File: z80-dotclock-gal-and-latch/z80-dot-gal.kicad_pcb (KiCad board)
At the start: 2 copper layers, 30.5 x 83.2 mm, 12 parts, among them J1 Board corner fix, J2 EXP_PORT, J3 GAL_1_9, J4 GAL_11_19, U1 Z80CPU SOCKET PINS, U2 Z80CPU, U3 GAL16V8

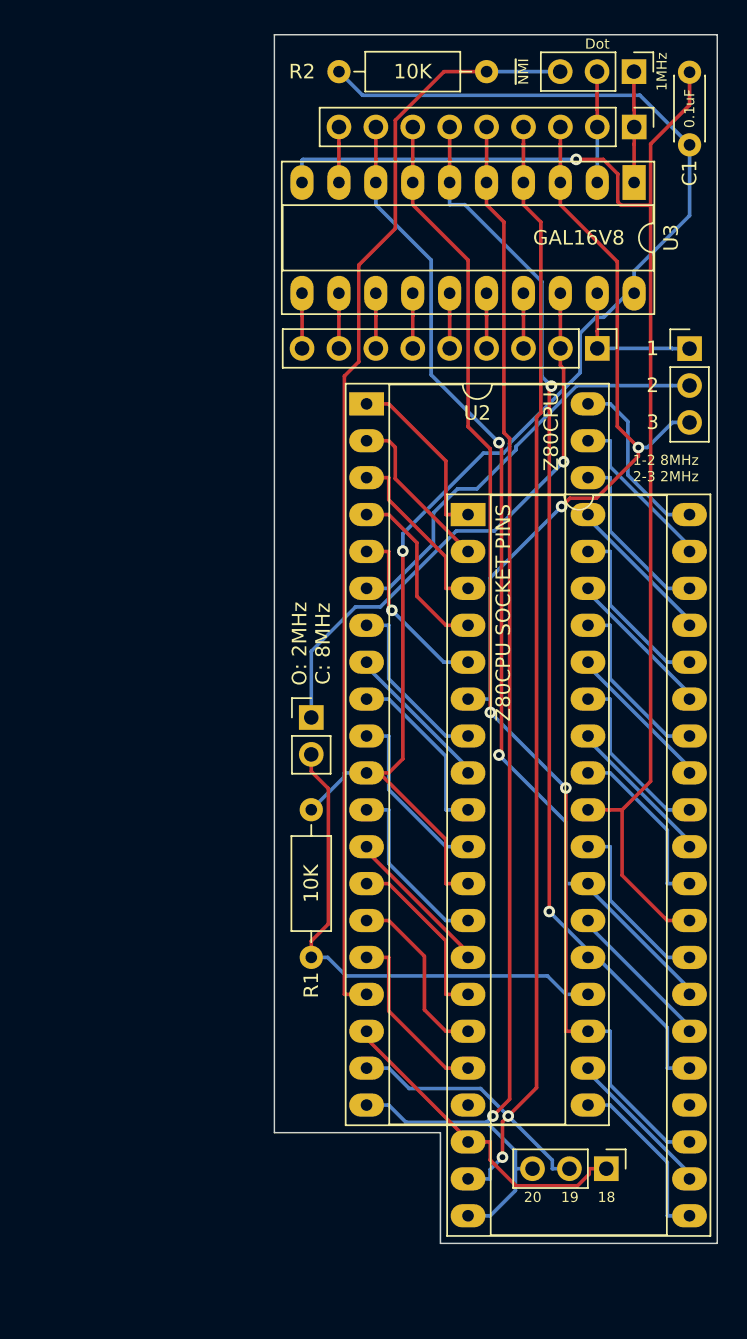
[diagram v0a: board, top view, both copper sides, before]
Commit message: Schematic revision v2, without PCB: - remove test pads - remove unused connections to GAL pins 6-8 - add J3 and lots of descriptions - add required connects to /WR, /RESET, /RFSH - make GAL socket compatible with 16V8
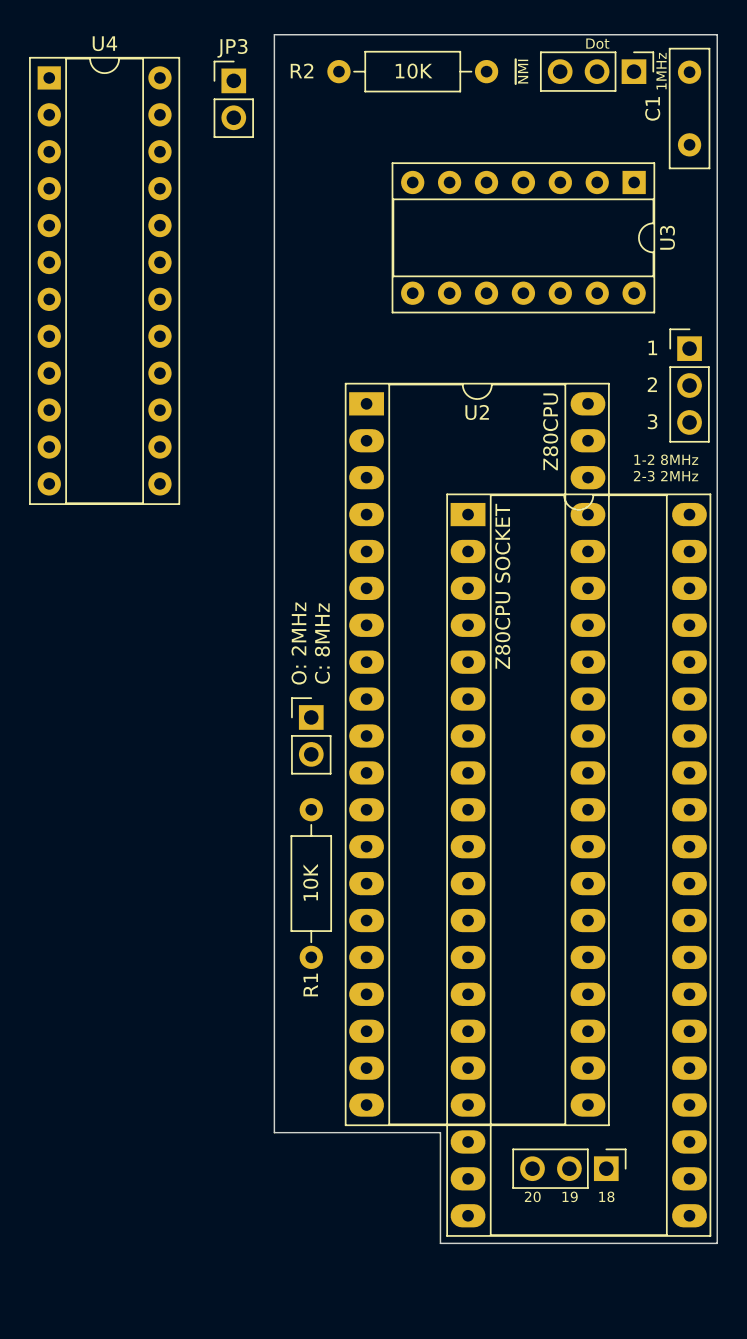
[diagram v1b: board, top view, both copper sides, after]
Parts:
- removed J3: GAL_1_9, Connector_PinHeader_2.54mm:PinHeader_1x09_P2.54mm_Vertical
- removed J4: GAL_11_19, Connector_PinHeader_2.54mm:PinHeader_1x09_P2.54mm_Vertical
- added JP3: FAST/SLOW, Connector_PinHeader_2.54mm:PinHeader_1x02_P2.54mm_Vertical, F.Cu at (111.5, 52.1)
- added U4: GAL22V10, Package_DIP:DIP-24_W7.62mm_Socket, F.Cu at (98.8, 51.9)
- C1: footprint Capacitor_THT:C_Disc_D4.3mm_W1.9mm_P5.00mm -> Capacitor_THT:C_Disc_D8.0mm_W2.5mm_P5.00mm
- U1: value Z80CPU SOCKET PINS -> Z80CPU SOCKET
- U3: value GAL16V8 -> 74LS74; footprint Package_DIP:DIP-20_W7.62mm_Socket_LongPads -> Package_DIP:DIP-14_W7.62mm_Socket
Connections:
- U3 pad 1: /CLK1MHZ -> /~{WAITRESET}
- U3 pad 10: GND -> VCC
- U3 pad 11: Net-(J4-Pad9) -> GND
- U3 pad 12: Net-(J4-Pad8) -> GND
- U3 pad 13: Net-(J4-Pad7) -> VCC
- U3 pad 14: Net-(J4-Pad6) -> VCC
- U3 pad 2: /DOTCLK -> VCC
- U3 pad 3: /~{CLK_IN} -> /WAITTRIGGER
- U3 pad 4: /~{MREQ} -> VCC
- U3 pad 5: /~{IORQ} -> unconnected-(U3-Pad5)
- U3 pad 6: /~{BUSRQ} -> /WAITLATCH
- U3 pad 7: /~{BUSACK} -> GND
- U3 pad 8: /~{M1} -> unconnected-(U3-Pad8)
- U3 pad 9: Net-(J3-Pad9) -> unconnected-(U3-Pad9)
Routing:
- net VCC: track 97.1 -> 0.00 mm, vias 1 -> 0
- net GND: track 93.5 -> 0.00 mm, vias 1 -> 0
- net /~{MREQ}: track 93.0 -> 0.00 mm, vias 2 -> 0
- net /~{IORQ}: track 89.2 -> 0.00 mm, vias 1 -> 0
- net /~{BUSACK}: track 81.2 -> 0.00 mm, vias 2 -> 0
- net /~{NMI}: track 75.9 -> 0.00 mm
- net /~{BUSRQ}: track 74.0 -> 0.00 mm, vias 2 -> 0
- net /~{M1}: track 69.7 -> 0.00 mm, vias 2 -> 0
- net /~{CLK_IN}: track 52.7 -> 0.00 mm, vias 2 -> 0
- net /~{WAITOUT}: track 39.0 -> 0.00 mm, vias 1 -> 0
- net /~{WAIT}: track 35.0 -> 0.00 mm
- net Net-(JP2-Pad2): track 29.4 -> 0.00 mm
- net /~{HALT}: track 22.7 -> 0.00 mm
- net /A15: track 12.4 -> 0.00 mm, vias 1 -> 0
- net /~{RD}: track 12.3 -> 0.00 mm
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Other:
- board text added: "C128 Z80 @ 8MHz V2.0 Maciej Witkowiak, <ytm@elysium.pl> VI 2024"
- board text removed: "C128 Z80 @ 8MHz dev board V1.0 Maciej Witkowiak, <ytm@elysium.pl> VIII 2023"

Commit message: C128D/DCR PCB project (without cutout for 256k MMU expansion)
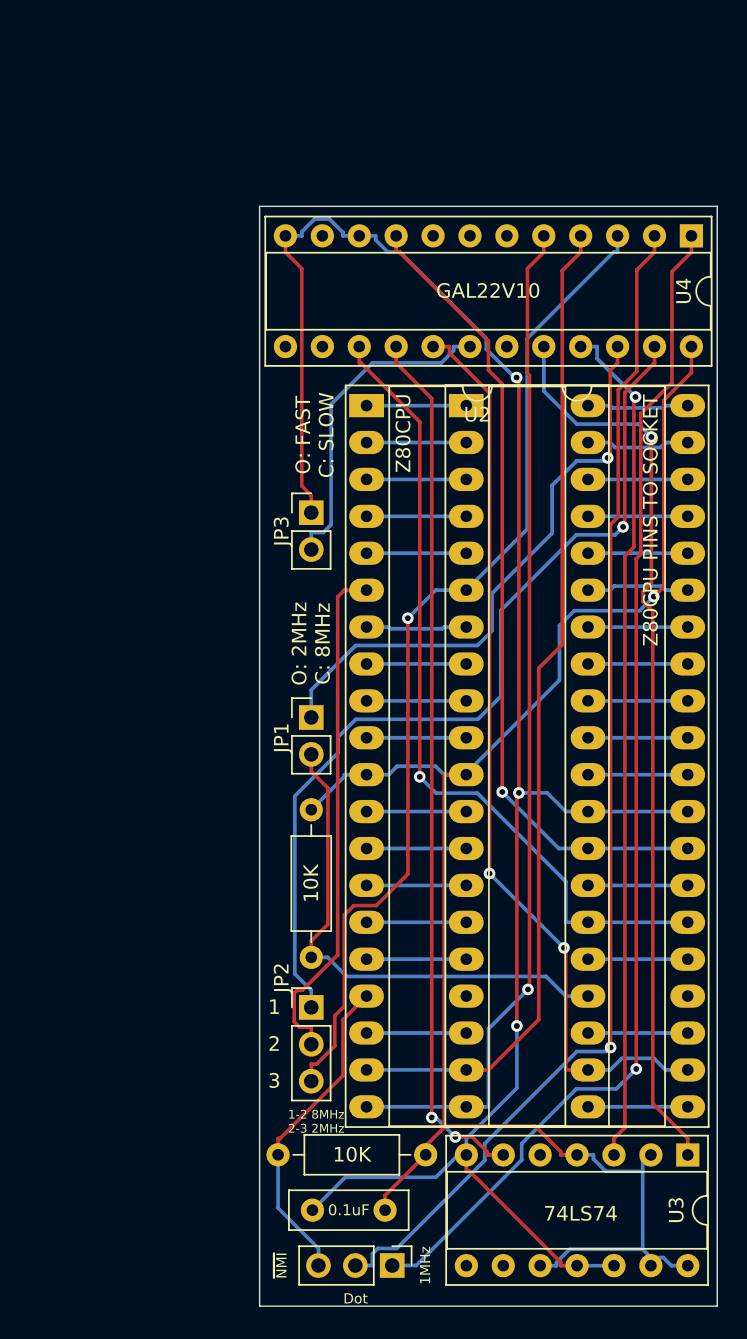
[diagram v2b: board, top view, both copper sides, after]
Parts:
- removed J1: Board corner fix, Connector_PinHeader_2.54mm:PinHeader_1x03_P2.54mm_Vertical
- U1: value Z80CPU SOCKET -> Z80CPU PINS TO SOCKET
- moved J2 83.8 mm to (122.4, 133.6)
- moved C1 76.3 mm to (121.9, 129.8), turned to 180 degrees
- moved R2 74.8 mm to (124.7, 126.0), turned to 180 degrees
- moved U3 67.0 mm to (142.8, 126.0)
- moved JP2 52.3 mm to (116.8, 115.8)
- moved U4 45.5 mm to (143.0, 62.7), turned to -90 degrees
- moved JP3 30.2 mm to (116.8, 81.8)
- moved U1 7.50 mm to (127.5, 74.4)
- moved U2 0.12 mm to (120.6, 74.4)
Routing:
- net GND: track 0.00 -> 135.3 mm, vias 0 -> 3
- net VCC: track 0.00 -> 118.1 mm, vias 0 -> 1
- net /DOTCLK: track 0.00 -> 82.0 mm, vias 0 -> 1
- net /CLK1MHZ: track 0.00 -> 82.0 mm, vias 0 -> 1
- net /~{IORQ}: track 0.00 -> 70.0 mm, vias 0 -> 1
- net /~{CLK_IN}: track 0.00 -> 69.4 mm, vias 0 -> 1
- net /~{MREQ}: track 0.00 -> 68.4 mm
- net /~{WR}: track 0.00 -> 63.3 mm, vias 0 -> 2
- net /~{WAITRESET}: track 0.00 -> 62.7 mm, vias 0 -> 1
- net /~{CLK_OUT}: track 0.00 -> 62.7 mm, vias 0 -> 1
- net /WAITLATCH: track 0.00 -> 60.2 mm, vias 0 -> 2
- net /WAITTRIGGER: track 0.00 -> 58.5 mm, vias 0 -> 1
- net /~{RFSH}: track 0.00 -> 55.8 mm, vias 0 -> 1
- net /~{RESET}: track 0.00 -> 55.6 mm, vias 0 -> 1
- net /~{WAITOUT}: track 0.00 -> 40.3 mm, vias 0 -> 1
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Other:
- board size 30.5 x 83.2 mm -> 31.5 x 75.7 mm
- board text added: "O: FAST C: SLOW"
- board text removed: "18"
- board text removed: "19"
- board text removed: "20"
